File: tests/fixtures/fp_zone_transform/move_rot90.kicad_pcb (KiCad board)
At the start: 2 copper layers, 45 x 40 mm, 1 part

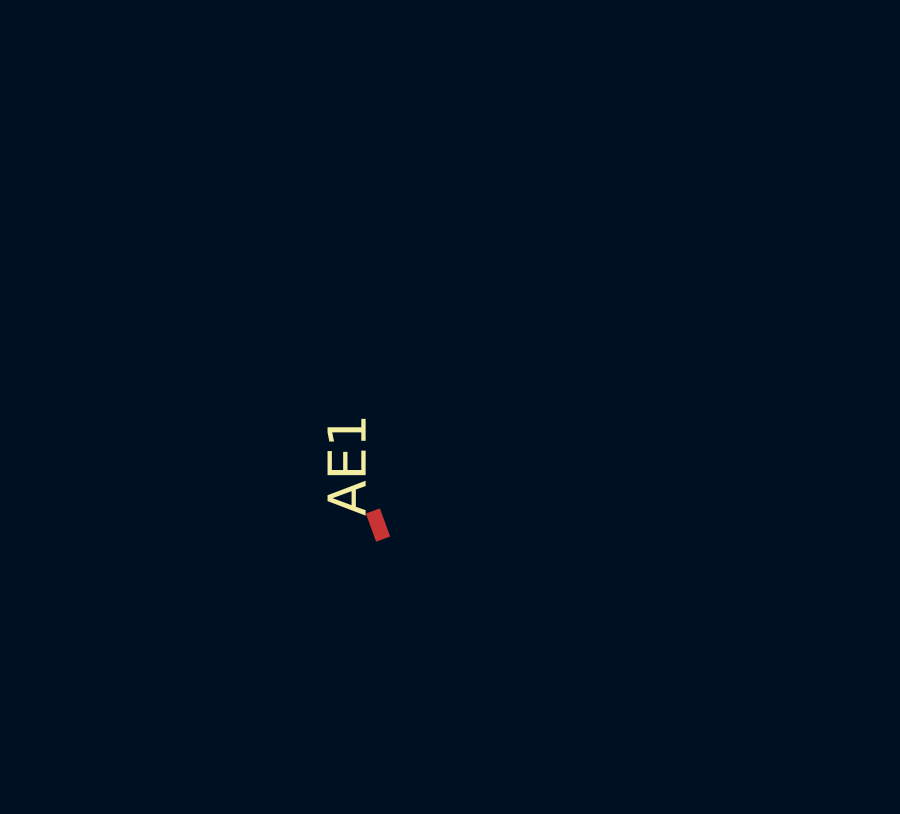
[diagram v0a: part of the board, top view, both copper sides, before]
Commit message: fix(pcb): turn footprint text angles with their footprint (#6126)
KiCad stores property/fp_text (at x y ANGLE) angles board-absolute, like
pad angles, so rotating or flipping a footprint must rewrite them. Pinned
against pcbnew 10.0.1 goldens (tests/fixtures/fp_zone_transform/, now
carrying keep-upright and unlocked user texts plus Rotate() cases):

- Footprint.__setattr__ maps text angles from the old placement frame to
  the new one (SetOrientation semantics: +delta on the same side, a -> -a
  under the left/right side swap), for both the S-expression nodes and the
  parsed FootprintText objects. This covers update_footprint_position,
  placement writeback, pcb move-footprint and snap-rotation.
- Footprint.keep_texts_upright / keep_footprint_texts_upright apply
  KiCad's FOOTPRINT::Rotate keep-upright step (>= 180 turns by -180 and
  swaps justification; (unlocked yes) / legacy `unlocked` texts are left
  alone). Used by pcb modify rotate, the recovery rotate strategy and the
  mirror strategy (pcb modify flip), replacing its `180 - a` text angle,
  which was 180 degrees off for unlocked and some keep-upright text.
- transform_footprint_text_nodes is the raw-node counterpart of
  transform_footprint_zone_nodes, used by pcb modify rotate.
- snap-rotation now turns pad angles by the snap amount.

Co-Authored-By: Claude Opus 5.5 (1M context) <noreply@anthropic.com>
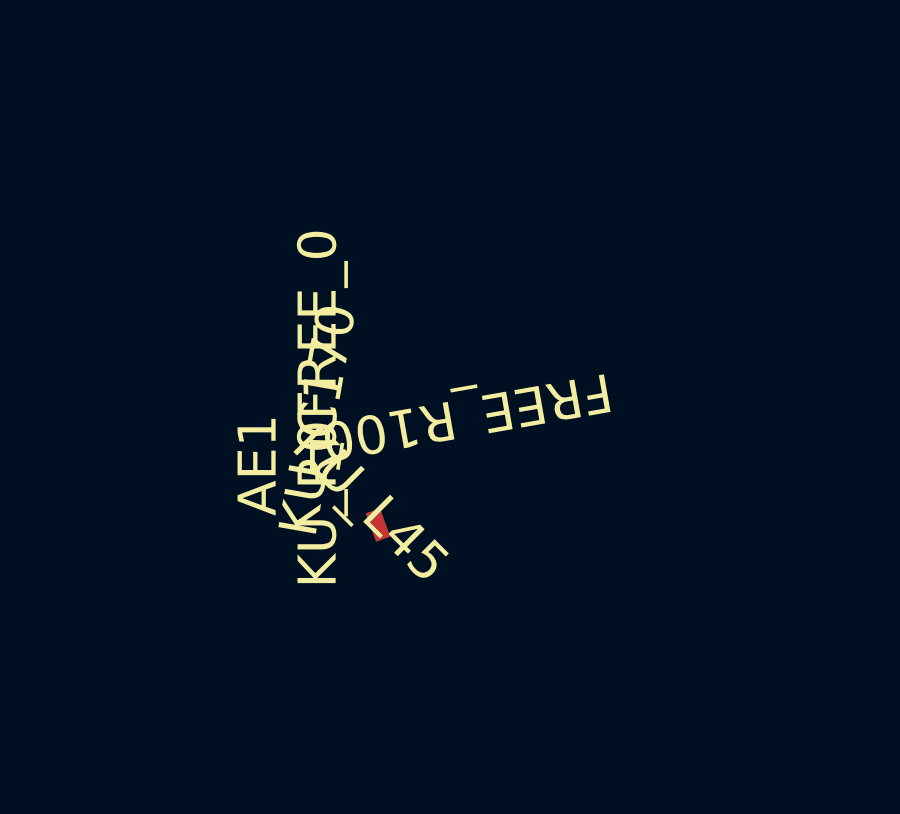
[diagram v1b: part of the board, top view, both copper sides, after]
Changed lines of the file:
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@@
 		(at 125 120 90)
 		(property "Reference" "AE1"
-			(at 0 0 90)
+			(at 0 -3 90)
 			(layer "F.SilkS")
 			(effects
@@
 		)
 		(property "Value" "ANTENNA"
-			(at 0 0 90)
+			(at 0.5 3 180)
 			(layer "F.Fab")
 			(effects
@@
 		)
 		(duplicate_pad_numbers_are_jumpers no)
+		(fp_text user "FREE_0"
+			(at 1.5 -1 90)
+			(unlocked yes)
+			(layer "F.SilkS")
+			(effects
+				(font
+					(size 1.27 1.27)
+				)
+				(justify left)
+			)
+		)
+		(fp_text user "KU_R0"
+			(at 1.5 -1 90)
+			(layer "F.SilkS")
+			(effects
+				(font
+					(size 1.27 1.27)
+				)
+				(justify right)
+			)
+		)
+		(fp_text user "KU_L45"
+			(at 1.5 -1 135)
+			(layer "F.SilkS")
+			(effects
+				(font
+					(size 1.27 1.27)
+				)
+				(justify left top)
+			)
+		)
+		(fp_text user "FREE_R100"
+			(at 1.5 -1 190)
+			(unlocked yes)
+			(layer "F.SilkS")
+			(effects
+				(font
+					(size 1.27 1.27)
+				)
+				(justify right bottom)
+			)
+		)
+		(fp_text user "KU_C170"
+			(at 1.5 -1 260)
+			(layer "F.SilkS")
+			(effects
+				(font
+					(size 1.27 1.27)
+				)
+			)
+		)
 		(pad "1" smd rect
 			(at -2 1 110)
